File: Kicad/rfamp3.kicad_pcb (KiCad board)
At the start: 2 copper layers, 149.4 x 60 mm, 69 parts, among them J1 Conn_Coaxial, J2 LPF-Out, J3 Conn_Coaxial, J4 LPF, J5 12V Power, J6 12V Switch, K1 G5V-2, K2 G5V-2, Q1 2N3906, Q2 RD6HHF1, Q3 IRF510, Q4 IRF510, T1 , T2 Transformer_1P_1S, T3 , U1 L7805

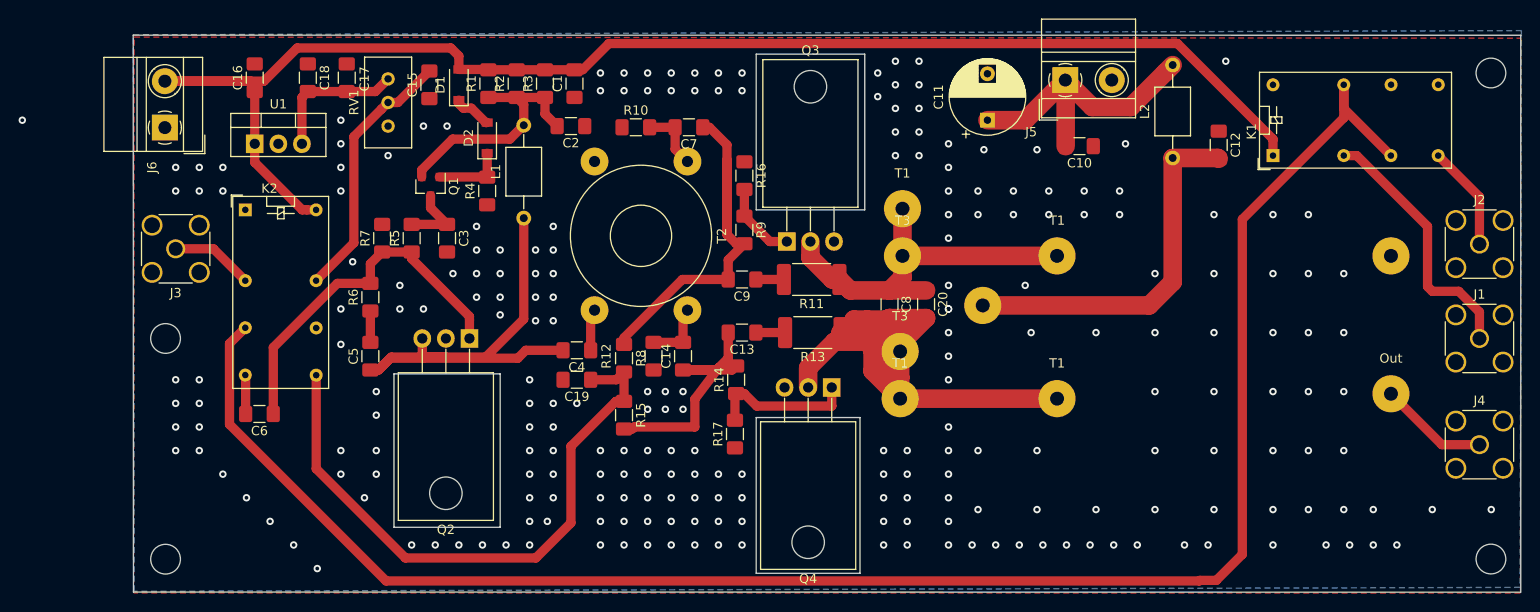
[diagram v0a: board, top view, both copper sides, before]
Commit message: add fly back diode
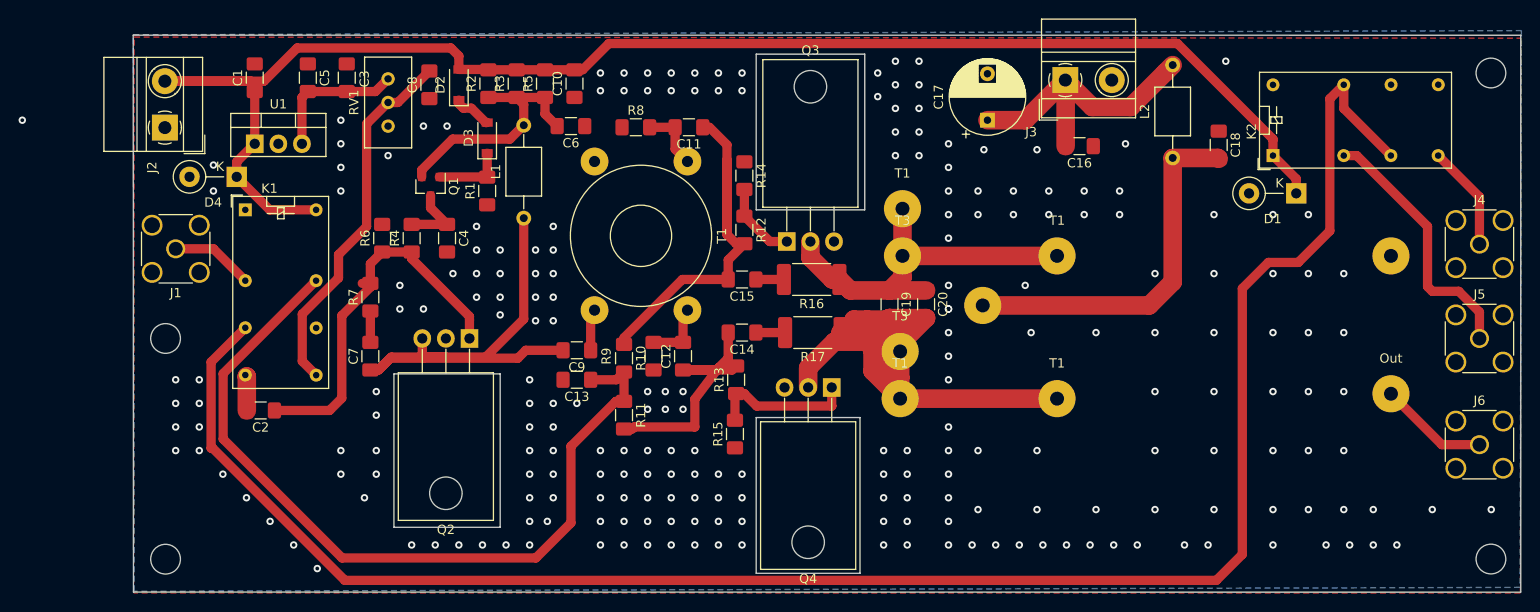
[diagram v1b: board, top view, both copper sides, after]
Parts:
- added D1: 1n4007, Diode_THT:D_DO-41_SOD81_P5.08mm_Vertical_KathodeUp, F.Cu at (186.7, 61.2)
- added D4: 1n4007, Diode_THT:D_DO-41_SOD81_P5.08mm_Vertical_KathodeUp, F.Cu at (72.6, 59.4)
- moved C2 0.40 mm to (75.2, 84.6)
- renumbered C16 to C1, C1 to C10, C7 to C11, C14 to C12, C19 to C13, C13 to C14, C9 to C15, C10 to C16, C11 to C17, C12 to C18, C8 to C19, C6 to C2, C17 to C3, C3 to C4, C18 to C5, C2 to C6, C5 to C7, C15 to C8, C4 to C9, D1 to D2, D2 to D3, J3 to J1, J6 to J2, J5 to J3, J2 to J4, J1 to J5, J4 to J6, K2 to K1, K1 to K2, R4 to R1, R8 to R10, R15 to R11, R9 to R12, R14 to R13, R16 to R14, R17 to R15, R11 to R16, R13 to R17, R1 to R2, R2 to R3, R5 to R4, R3 to R5, R7 to R6, R6 to R7, R10 to R8, R12 to R9, T2 to T1
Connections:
- C12 pad 2: Net-(C14-Pad2) -> Net-(C12-Pad2)
- C18 pad 2: Net-(C12-Pad2) -> Net-(C18-Pad2)
- C19 pad 1: Net-(C20-Pad1) -> Net-(C19-Pad1)
- C19 pad 2: Net-(C20-Pad2) -> Net-(C19-Pad2)
- C20 pad 1: Net-(C20-Pad1) -> Net-(C19-Pad1)
- C20 pad 2: Net-(C20-Pad2) -> Net-(C19-Pad2)
- C8 pad 2: Net-(C15-Pad2) -> Net-(C8-Pad2)
- J4 pad 1: Net-(J2-Pad1) -> Net-(J4-Pad1)
- J6 pad 1: Net-(J4-Pad1) -> Net-(J6-Pad1)
- K1 pad 13: Net-(C15-Pad2) -> Bias_A
- K1 pad 9: Bias_A -> Net-(C8-Pad2)
- K2 pad 11: Net-(K1-Pad11) -> unconnected-(K2-Pad11)
- K2 pad 8: Net-(J2-Pad1) -> Net-(J4-Pad1)
- L2 pad 1: Net-(C12-Pad2) -> Net-(C18-Pad2)
- Q3 pad 2: Net-(C20-Pad1) -> Net-(C19-Pad1)
- Q4 pad 2: Net-(C20-Pad2) -> Net-(C19-Pad2)
- R16 pad 1: Net-(C20-Pad1) -> Net-(C19-Pad1)
- R17 pad 1: Net-(C20-Pad2) -> Net-(C19-Pad2)
- R9 pad 2: Net-(C14-Pad2) -> Net-(C12-Pad2)
- RV1 pad 2: Net-(C15-Pad2) -> Net-(C8-Pad2)
- T1 pad 4: Net-(C14-Pad2) -> Net-(C12-Pad2)
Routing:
- net Net-(C20-Pad2): track 82.3 -> 0.00 mm
- net Net-(C19-Pad2): track 0.00 -> 82.3 mm
- net Net-(C20-Pad1): track 41.7 -> 0.00 mm
- net Net-(C19-Pad1): track 0.00 -> 41.7 mm
- net Net-(C18-Pad2): track 0.00 -> 39.8 mm
- net Net-(C8-Pad2): track 0.00 -> 39.6 mm
- net Net-(C12-Pad2): track 39.8 -> 6.84 mm
- net Net-(C15-Pad2): track 28.2 -> 0.00 mm
- net Bias_A: track 66.1 -> 88.6 mm
- net Net-(J6-Pad1): track 0.00 -> 11.8 mm
- net Net-(J2-Pad1): track 11.4 -> 0.00 mm
- net 12V_Switch: track 156.7 -> 165.4 mm, vias 0 -> 1
- net Net-(C14-Pad2): track 6.84 -> 0.00 mm
- net Net-(K1-Pad6): track 193.1 -> 199.2 mm
- net Net-(C2-Pad1): track 39.4 -> 41.3 mm
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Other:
- net class Default removed
- net class Power removed
- net class Power2 removed
- net class Power3 removed
